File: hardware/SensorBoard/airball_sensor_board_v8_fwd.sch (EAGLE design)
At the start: 60 parts, among them IC1 CP2102, J2 USB Female Type C Connector, T1 BC846, T2 BC846, U1 BQ24075, U2 BQ27441-G1, U3 BMP388, U4 ESP-WROOM-32

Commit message: Finished initial design and routing.
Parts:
- removed FID1, FID2, FID3, FID4, FID5, FID6: FIDUCIAL1X2, SparkFun-Aesthetics:FIDUCIAL1X2
- removed FRAME1, FRAME2: FRAME-LETTER, SparkFun-Aesthetics:FRAME-LETTER
- removed R11: (no value), SparkFun-Resistors:RESISTOR1206
- removed STANDOFF1, STANDOFF10, STANDOFF11, STANDOFF12, STANDOFF2, STANDOFF3, STANDOFF4, STANDOFF5, STANDOFF6, STANDOFF7, STANDOFF8, STANDOFF9: STAND-OFF, SparkFun-Electromechanical:STAND-OFF
- added C10: 10uF, SparkFun-Capacitors:10UF-0603-6.3V-20%
- added C11, C925, C926, C927: 4.7uF, SparkFun-Capacitors:4.7UF-0603-6.3V-(10%)
- added C8, C9: 0.1uF, SparkFun-Capacitors:0.1UF-0603-25V-(+80/-20%)
- added R17: 0.01, SparkFun-Resistors:RESISTOR1206
- added U7: SP0503BAHT, SP0503BAHT:SP0503BAHT
- R3: value 2.0k -> 1k; device SparkFun-Resistors:2.0KOHM-0603-1/10W-5% -> SparkFun-Resistors:1KOHM-0603-1/10W-1%
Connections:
- net N$1 renamed MISO
- net N$10 renamed SS_27
- net N$2 renamed SCLK
- net N$6 renamed SS_25
- net N$9 renamed SS_26
- new net N$14: C6.1, U2.VDD
- net BATTERY_IN: now also R17.2; no longer R11.2
- net GND: now also C10.2, C11.2, C8.2, C9.2, C925.2, C926.2, C927.2, J1.1, U7.GND; no longer J1.2
- net USB_D+: now also U7.B
- net USB_D-: now also U7.A
- net VCC: now also C10.1, C11.1, C8.1, C9.1, C925.1, C926.1, C927.1, J1.2, U3.VDD; no longer C6.1, J1.1, R3.2, U2.VDD
- net V_BATT: now also R17.1; no longer R11.1
- net V_USB: now also R3.2, U7.C
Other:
- note removed: "1/3"
- note removed: "2/3"
- note removed: "3/3"
- moved on the sheet: C7, IC1, R10, R12, R13, R14, R3, R4, R6, T1, T2, U3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

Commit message: More routing and design.
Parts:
- added D2: GREEN, SparkFun-LED:LED-GREEN0603
- added D3: Yellow, SparkFun-LED:LED-YELLOW0603
- added D4: RED, SparkFun-LED:LED-RED0603
- added R11: 180, SparkFun-Resistors:180OHM1/10W1%(0603)
- added R18: 10K, SparkFun-Resistors:10KOHM-1/10W-1%(0603)0603
- added R19: 750, SparkFun-Resistors:10KOHM-1/10W-1%(0603)0603
- R5: value 590 -> 898
- R7: value 1.1k -> 1.54k
- R8: value 100k -> 750; device SparkFun-Resistors:100KOHM-1/10W-1%(0603) -> SparkFun-Resistors:10KOHM-1/10W-1%(0603)0603
- U$925, U$926, U$927: value HONEYWELL_HSC_SMT -> (none)
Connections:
- net N$3 renamed SYSOFF_PULLUP
- removed net !CE!: R8.1, U1.!CE!
- removed net EN1: R16.2, U1.EN1
- new net N$1: D4.A, U4.IO33
- new net N$19: R11.2, U1.!PGOOD!
- new net N$2: D4.C, R19.1
- new net N$20: D2.C, R11.1
- new net N$21: R16.2, U1.EN2
- new net N$22: D3.C, R8.1
- new net N$23: R18.2, U2.BIN
- net GND: now also R18.1, R19.2, U1.!CE!, U1.EN1; no longer U1.EN2
- net TS: no longer U2.BIN
- net VCC: now also D3.A
- net V_SUPPLY_UNREG: now also D2.A
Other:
- note added: "C1 is 1206 50V Cap for USB input only"
- note added: "D1 = Charging D2 = USB power available D3 = System powered on"
- note added: "R17 is 1206 Current Sense Resistor"
- moved on the sheet: C1, C5, C6, R1, R13, R14, R17, R8, S1, T1, T2, U2

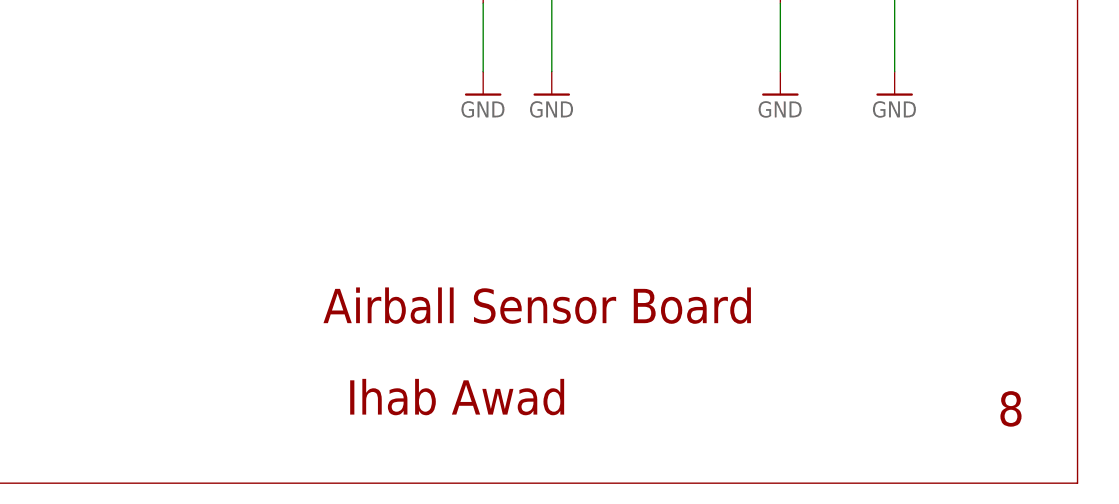
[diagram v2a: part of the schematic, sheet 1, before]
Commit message: Updated descriptions and documentation.
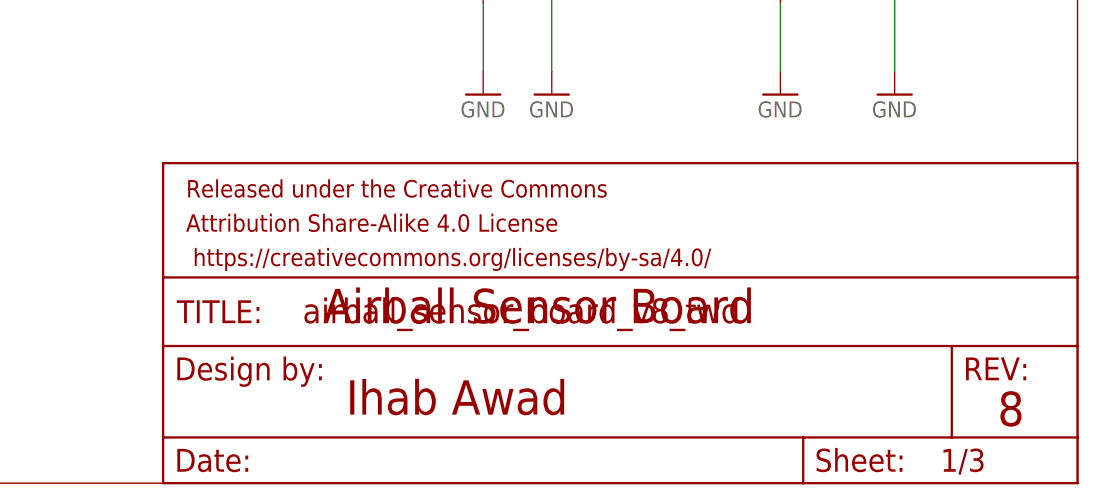
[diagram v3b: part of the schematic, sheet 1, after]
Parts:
- added FRAME1, FRAME2: FRAME-LETTER, SparkFun-Aesthetics:FRAME-LETTER
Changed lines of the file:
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@@
 <part name="R19" library="SparkFun-Resistors" deviceset="10KOHM-1/10W-1%(0603)" device="0603" value="750"/>
 <part name="GND32" library="SparkFun-PowerSymbols" deviceset="GND" device=""/>
+<part name="FRAME1" library="SparkFun-Aesthetics" deviceset="FRAME-LETTER" device=""/>
+<part name="FRAME2" library="SparkFun-Aesthetics" deviceset="FRAME-LETTER" device=""/>
 </parts>
 <sheets>
@@
 <text x="167.64" y="17.78" size="3.81" layer="94">Airball Sensor Board</text>
 <text x="170.18" y="7.62" size="3.81" layer="94">Ihab Awad</text>
-<text x="242.57" y="6.35" size="3.81" layer="94">8</text>
 <text x="17.78" y="60.96" size="1.778" layer="94">C1 is 1206 50V
 Cap for USB
@@
 D2 = USB power available
 D3 = System powered on</text>
+<text x="242.57" y="6.35" size="3.81" layer="94">8</text>
 </plain>
 <instances>
@@
 <attribute name="VALUE" x="231.14" y="114.3" size="1.778" layer="96"/>
 </instance>
+<instance part="FRAME2" gate="V" x="149.86" y="0" smashed="yes"/>
 </instances>
 <busses>
@@
 <attribute name="VALUE" x="101.6" y="63.5" size="1.778" layer="96"/>
 </instance>
+<instance part="FRAME1" gate="V" x="152.4" y="0" smashed="yes"/>
 </instances>
 <busses>
